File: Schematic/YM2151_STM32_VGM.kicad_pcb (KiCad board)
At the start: 2 copper layers, 156.8 x 67.3 mm, 52 parts, among them J1 DM3CS-SF (Micro SD Card Slot), J2 Jack_DC+12V, J3 JACK_TRS_6PINS, J4 USB_B, SW1 PWR_SWITCH, SW2 MUTE_SWITCH, SW3 PREV, SW4 RAND, SW5 NEXT, SW6 LOOP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

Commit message: PCB complete
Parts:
- moved C2 2.69 mm to (147.3, 52.7), turned to 180 degrees
- moved C1 1.27 mm to (149.9, 57.1)
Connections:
- J3 pad 1: GND -> L_OUT
- J3 pad 2: L_OUT -> R_OUT
- J3 pad 3: R_OUT -> GND
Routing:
- net +5V: track 239.4 -> 242.3 mm
- net L_OUT: track 19.6 -> 21.9 mm
- net R_OUT: track 16.3 -> 15.0 mm
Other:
- board text added: "LET'S ROCK!"
- board text added: "OFF"
- board text added: "ON"
- board text added: "PORT END"
- board text added: "YM2151 Arcade Classic VGM Player 2018 Aidan Lawrence www.aidanlawrence.com"

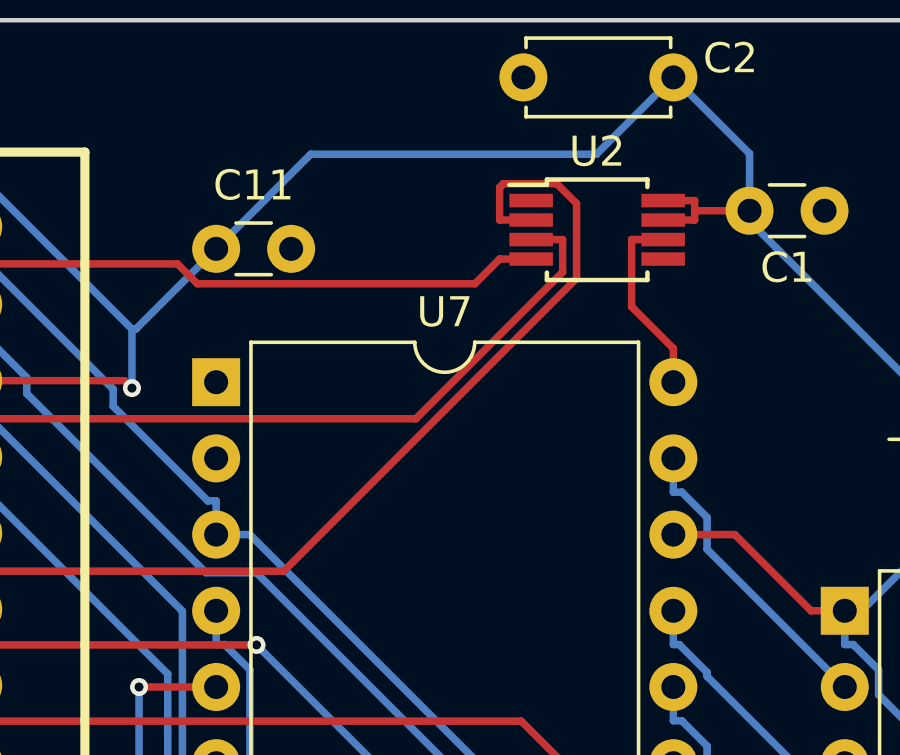
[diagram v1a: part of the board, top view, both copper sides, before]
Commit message: Corrected PCB - unconnected GND on LTC6903
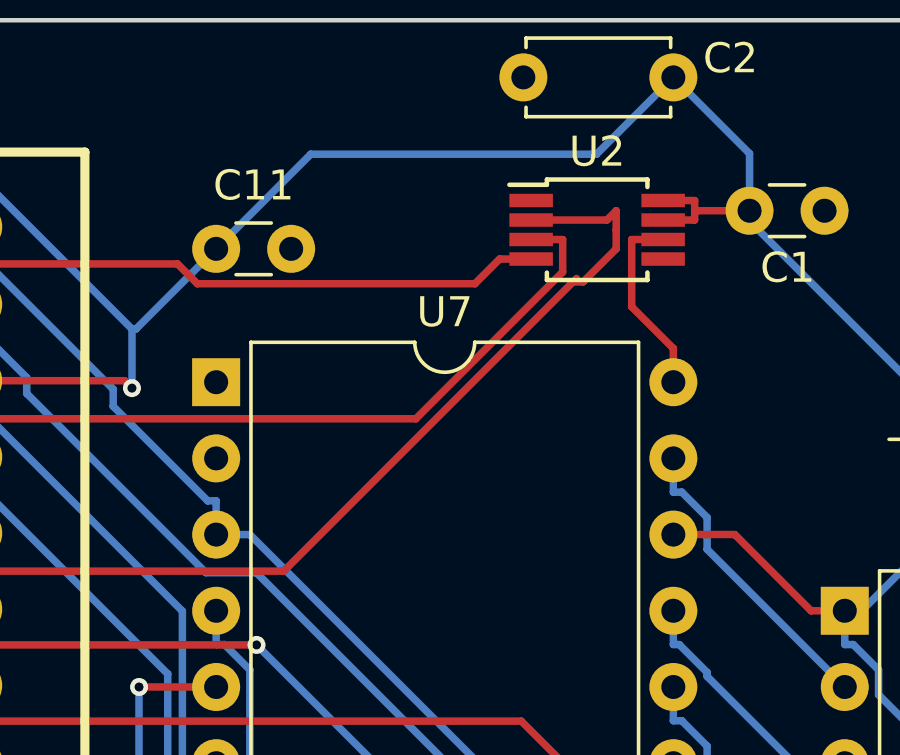
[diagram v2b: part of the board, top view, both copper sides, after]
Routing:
- net SPI_MOSI: track 74.5 -> 73.1 mm
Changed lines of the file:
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@@
     (links 160)
     (no_connects 1)
-    (area 72.314999 50.724999 229.310001 118.185001)
+    (area 69.85 47.625 235.585001 120.650001)
     (thickness 1.6)
     (drawings 26)
-    (tracks 550)
+    (tracks 551)
     (zones 0)
     (modules 52)
@@
   (segment (start 103.0268 77.8345) (end 97.9051 72.7128) (width 0.25) (layer B.Cu) (net 27))
   (segment (start 103.0268 78.0542) (end 103.0268 77.8345) (width 0.25) (layer B.Cu) (net 27))
+  (segment (start 145.415 57.785) (end 145.415 57.15) (width 0.25) (layer F.Cu) (net 28))
+  (segment (start 143.9772 59.5222) (end 144.3128 59.5222) (width 0.25) (layer F.Cu) (net 28))
+  (segment (start 144.3128 59.5222) (end 145.415 58.42) (width 0.25) (layer F.Cu) (net 28))
+  (segment (start 145.415 58.42) (end 145.415 57.785) (width 0.25) (layer F.Cu) (net 28))
+  (segment (start 145.105 57.46) (end 142.58 57.46) (width 0.25) (layer F.Cu) (net 28))
+  (segment (start 145.415 57.15) (end 145.105 57.46) (width 0.25) (layer F.Cu) (net 28))
   (segment (start 102.6061 69.1642) (end 101.3153 70.455) (width 0.25) (layer F.Cu) (net 28))
   (segment (start 134.3352 69.1642) (end 102.6061 69.1642) (width 0.25) (layer F.Cu) (net 28))
-  (segment (start 144.0936 59.4058) (end 134.3352 69.1642) (width 0.25) (layer F.Cu) (net 28))
-  (segment (start 144.0936 56.9082) (end 144.0936 59.4058) (width 0.25) (layer F.Cu) (net 28))
-  (segment (start 143.4358 56.2504) (end 144.0936 56.9082) (width 0.25) (layer F.Cu) (net 28))
-  (segment (start 141.6526 56.2504) (end 143.4358 56.2504) (width 0.25) (layer F.Cu) (net 28))
-  (segment (start 141.5297 56.3733) (end 141.6526 56.2504) (width 0.25) (layer F.Cu) (net 28))
-  (segment (start 141.5297 57.46) (end 141.5297 56.3733) (width 0.25) (layer F.Cu) (net 28))
-  (segment (start 142.58 57.46) (end 141.5297 57.46) (width 0.25) (layer F.Cu) (net 28))
+  (segment (start 144.0936 59.4058) (end 143.9772 59.5222) (width 0.25) (layer F.Cu) (net 28))
+  (segment (start 143.9772 59.5222) (end 134.3352 69.1642) (width 0.25) (layer F.Cu) (net 28))
   (segment (start 100.24 70.455) (end 101.3153 70.455) (width 0.25) (layer F.Cu) (net 28))
   (segment (start 101.3153 77.81) (end 101.3153 70.455) (width 0.25) (layer F.Cu) (net 28))

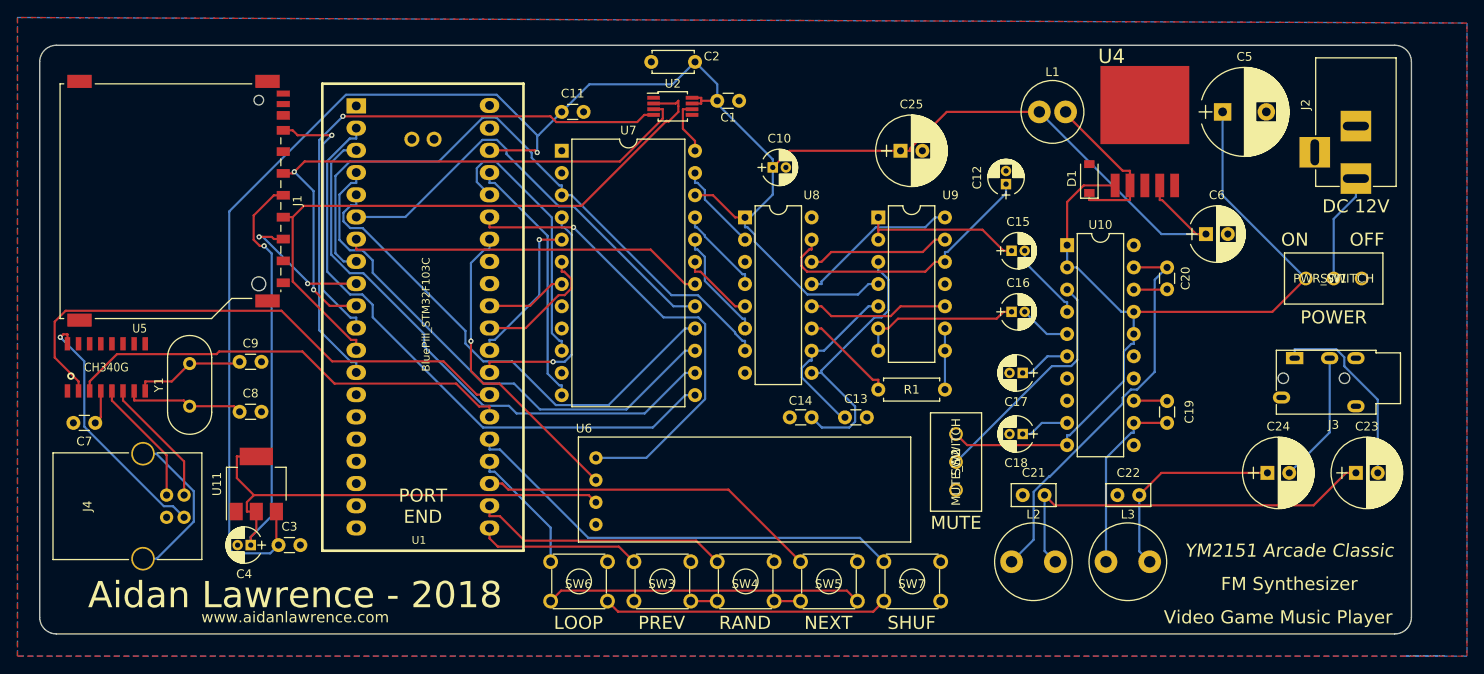
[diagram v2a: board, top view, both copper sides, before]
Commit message: Corrected SD card on schematic and board. Added button control
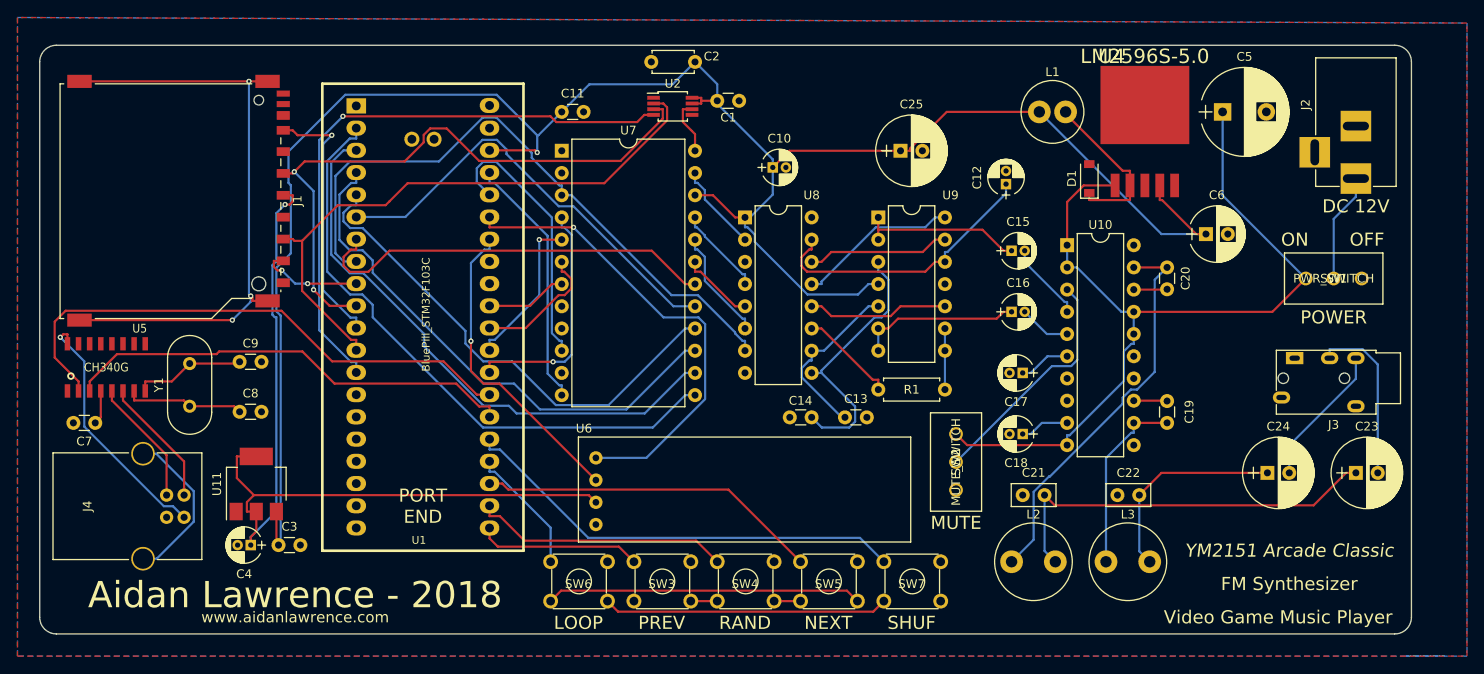
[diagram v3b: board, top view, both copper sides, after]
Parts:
- J1: value DM3CS-SF (Micro SD Card Slot) -> SD_Card
- U4: value (none) -> LM2596S-5.0
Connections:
- J1 pad 1: Net-(J1-Pad1) -> SD_CS
- J1 pad 10: (no net) -> Net-(J1-Pad10)
- J1 pad 11: (no net) -> Net-(J1-Pad11)
- J1 pad 12: (no net) -> Net-(J1-Pad12)
- J1 pad 2: SD_CS -> SPI_MOSI
- J1 pad 3: SPI_MOSI -> GND
- J3 pad 1: L_OUT -> GND
- J3 pad 2: R_OUT -> L_OUT
- J3 pad 3: GND -> R_OUT
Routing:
- net Net-(J1-Pad12): track 0.00 -> 69.6 mm, vias 0 -> 3
- net +5V: track 242.3 -> 234.0 mm
- net D7: track 41.6 -> 47.1 mm
- net SPI_MOSI: track 73.1 -> 68.3 mm
- net SD_CS: track 16.3 -> 12.0 mm
- net SPI_SCLK: track 68.2 -> 71.7 mm
- net L_OUT: track 21.9 -> 19.6 mm
- net R_OUT: track 15.0 -> 16.3 mm

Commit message: Repaired headphone jack pinout on PCB.
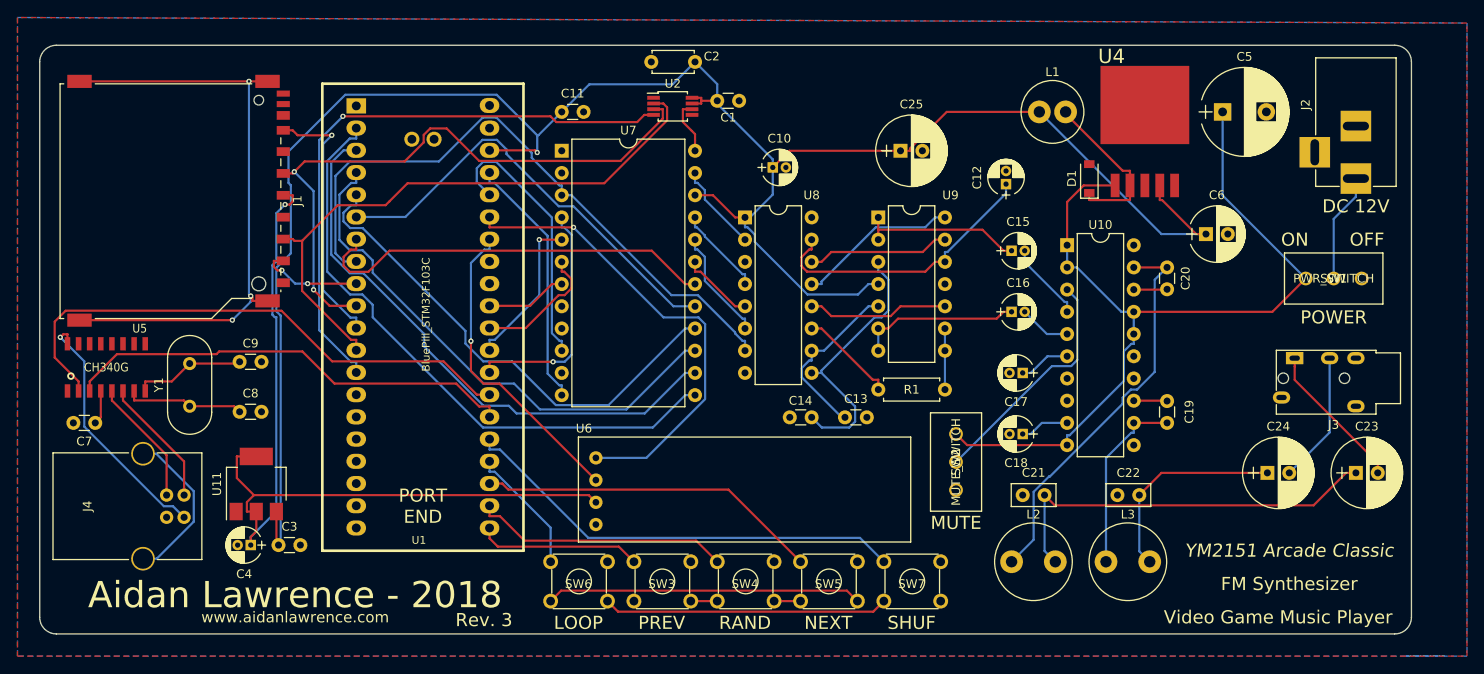
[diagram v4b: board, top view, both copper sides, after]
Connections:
- J3 pad 1: GND -> L_OUT
- J3 pad 2: L_OUT -> R_OUT
- J3 pad 3: R_OUT -> GND
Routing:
- net L_OUT: track 19.6 -> 17.1 mm
- net R_OUT: track 16.3 -> 15.0 mm
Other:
- board text added: "Rev. 3"
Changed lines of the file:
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@@
-(kicad_pcb (version 4) (host pcbnew 4.0.7)
+(kicad_pcb (version 20171130) (host pcbnew "(5.0.0-rc2-dev-493-gd776eaca8)")
   (general
-    (links 164)
-    (no_connects 1)
-    (area 69.85 47.625 235.585001 120.650001)
     (thickness 1.6)
-    (drawings 26)
-    (tracks 586)
+    (drawings 27)
+    (tracks 585)
     (zones 0)
     (modules 52)
@@
     (visible_elements 7FFFFFFF)
     (pcbplotparams
-      (layerselection 0x010fc_80000001)
+      (layerselection 0x010fc_ffffffff)
       (usegerberextensions false)
-      (excludeedgelayer true)
-      (linewidth 0.100000)
+      (usegerberattributes true)
+      (usegerberadvancedattributes false)
+      (creategerberjobfile false)
+      (excludeedgelayer false)
+      (linewidth 0.150000)
       (plotframeref false)
       (viasonmask false)
@@
       (hpglpenspeed 20)
       (hpglpendiameter 15)
-      (hpglpenoverlay 2)
       (psnegative false)
       (psa4output false)
@@
     (descr "DC Barrel Jack")
     (tags "Power Jack")
-    (fp_text reference J2 (at -8.45 5.75 450) (layer F.SilkS)
+    (fp_text reference J2 (at -8.45 5.75 90) (layer F.SilkS)
       (effects (font (size 1 1) (thickness 0.15)))
     )
@@
     (descr "Headphones with microphone connector, 3.5mm, 4 pins.")
     (tags "3.5mm jack mic microphone phones headphones 4pins audio plug")
-    (fp_text reference J3 (at 7.62 -4.445 360) (layer F.SilkS)
+    (fp_text reference J3 (at 7.62 -4.445) (layer F.SilkS)
       (effects (font (size 1 1) (thickness 0.15)))
     )
@@
       (effects (font (size 1 1) (thickness 0.15)))
     )
-    (fp_text user %R (at 7.62 -4.445 360) (layer F.Fab)
+    (fp_text user %R (at 7.62 -4.445) (layer F.Fab)
       (effects (font (size 1 1) (thickness 0.15)))
     )
@@
       (net 34 "Net-(J3-Pad4)"))
     (pad 1 thru_hole rect (at 0 0 180) (size 2 1.4) (drill oval 1.2 0.6) (layers *.Cu *.Mask)
-      (net 2 GND))
-    (pad 2 thru_hole oval (at 0 -4 180) (size 2 1.4) (drill oval 1.2 0.6) (layers *.Cu *.Mask)
       (net 23 L_OUT))
-    (pad 3 thru_hole oval (at 0 -7 180) (size 2 1.4) (drill oval 1.2 0.6) (layers *.Cu *.Mask)
+    (pad 2 thru_hole oval (at 0 -4 180) (size 2 1.4) (drill oval 1.2 0.6) (layers *.Cu *.Mask)
       (net 24 R_OUT))
+    (pad 3 thru_hole oval (at 0 -7 180) (size 2 1.4) (drill oval 1.2 0.6) (layers *.Cu *.Mask)
+      (net 2 GND))
     (pad "" np_thru_hole circle (at 2.3 -5.7 180) (size 1.2 1.2) (drill 1.2) (layers *.Cu *.Mask))
     (pad "" np_thru_hole circle (at 2.3 1.3 180) (size 1.2 1.2) (drill 1.2) (layers *.Cu *.Mask))
@@
       (net 38 "Net-(J4-Pad5)"))
     (model ${KISYS3DMOD}/Connectors.3dshapes/USB_B.wrl
-      (at (xyz 0.18 -0.05 0))
+      (offset (xyz 4.571999931335449 -1.269999980926514 0))
       (scale (xyz 0.39 0.39 0.39))
       (rotate (xyz 0 0 -90))
@@
       (effects (font (size 1.64501 1.64501) (thickness 0.05)))
     )
-    (fp_text value LM2596S-5.0 (at 0 -5.715) (layer F.SilkS)
+    (fp_text value LM2596S-5.0 (at 0 -5.715) (layer F.SilkS) hide
       (effects (font (size 1.64347 1.64347) (thickness 0.05)))
     )
@@
     )
   )
+  (gr_text "Rev. 3" (at 123.19 116.5225) (layer F.SilkS)
+    (effects (font (size 1.5 1.5) (thickness 0.3)))
+  )
   (gr_text OFF (at 224.155 73.025) (layer F.SilkS)
     (effects (font (size 1.5 1.5) (thickness 0.3)))
@@
   (segment (start 200.66 99.695) (end 198.12 102.235) (width 0.25) (layer F.Cu) (net 22))
   (segment (start 212.765 99.695) (end 200.66 99.695) (width 0.25) (layer F.Cu) (net 22))
-  (segment (start 225.385 87.2925) (end 225.385 99.695) (width 0.25) (layer B.Cu) (net 23))
-  (segment (start 223.6422 85.5497) (end 225.385 87.2925) (width 0.25) (layer B.Cu) (net 23))
-  (segment (start 219.885 85.5497) (end 223.6422 85.5497) (width 0.25) (layer B.Cu) (net 23))
-  (segment (start 219.885 86.575) (end 219.885 85.5497) (width 0.25) (layer B.Cu) (net 23))
-  (segment (start 215.265 96.554) (end 215.265 99.695) (width 0.25) (layer B.Cu) (net 24))
-  (segment (start 222.885 88.934) (end 215.265 96.554) (width 0.25) (layer B.Cu) (net 24))
-  (segment (start 222.885 86.575) (end 222.885 88.934) (width 0.25) (layer B.Cu) (net 24))
+  (segment (start 215.885 87.525) (end 215.885 86.575) (width 0.25) (layer F.Cu) (net 23))
+  (segment (start 225.385 99.695) (end 225.385 98.56363) (width 0.25) (layer F.Cu) (net 23))
+  (segment (start 215.885 89.06363) (end 215.885 87.525) (width 0.25) (layer F.Cu) (net 23))
+  (segment (start 225.385 98.56363) (end 215.885 89.06363) (width 0.25) (layer F.Cu) (net 23))
+  (segment (start 219.885 95.075) (end 219.885 86.575) (width 0.25) (layer B.Cu) (net 24))
+  (segment (start 215.265 99.695) (end 219.885 95.075) (width 0.25) (layer B.Cu) (net 24))
   (segment (start 192.4386 68.4989) (end 197.0532 68.4989) (width 0.25) (layer F.Cu) (net 25))
   (segment (start 192.405 68.4653) (end 192.4386 68.4989) (width 0.25) (layer F.Cu) (net 25))
